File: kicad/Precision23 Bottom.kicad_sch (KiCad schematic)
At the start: 13 parts, among them J396 STANDOFF, J397 STANDOFF, J398 STANDOFF, J399 STANDOFF, J507 Conn_01x06, J895 USB A Male to Blank, U801 Arduino Nano 33 IoT, U802 TXS0108EPW

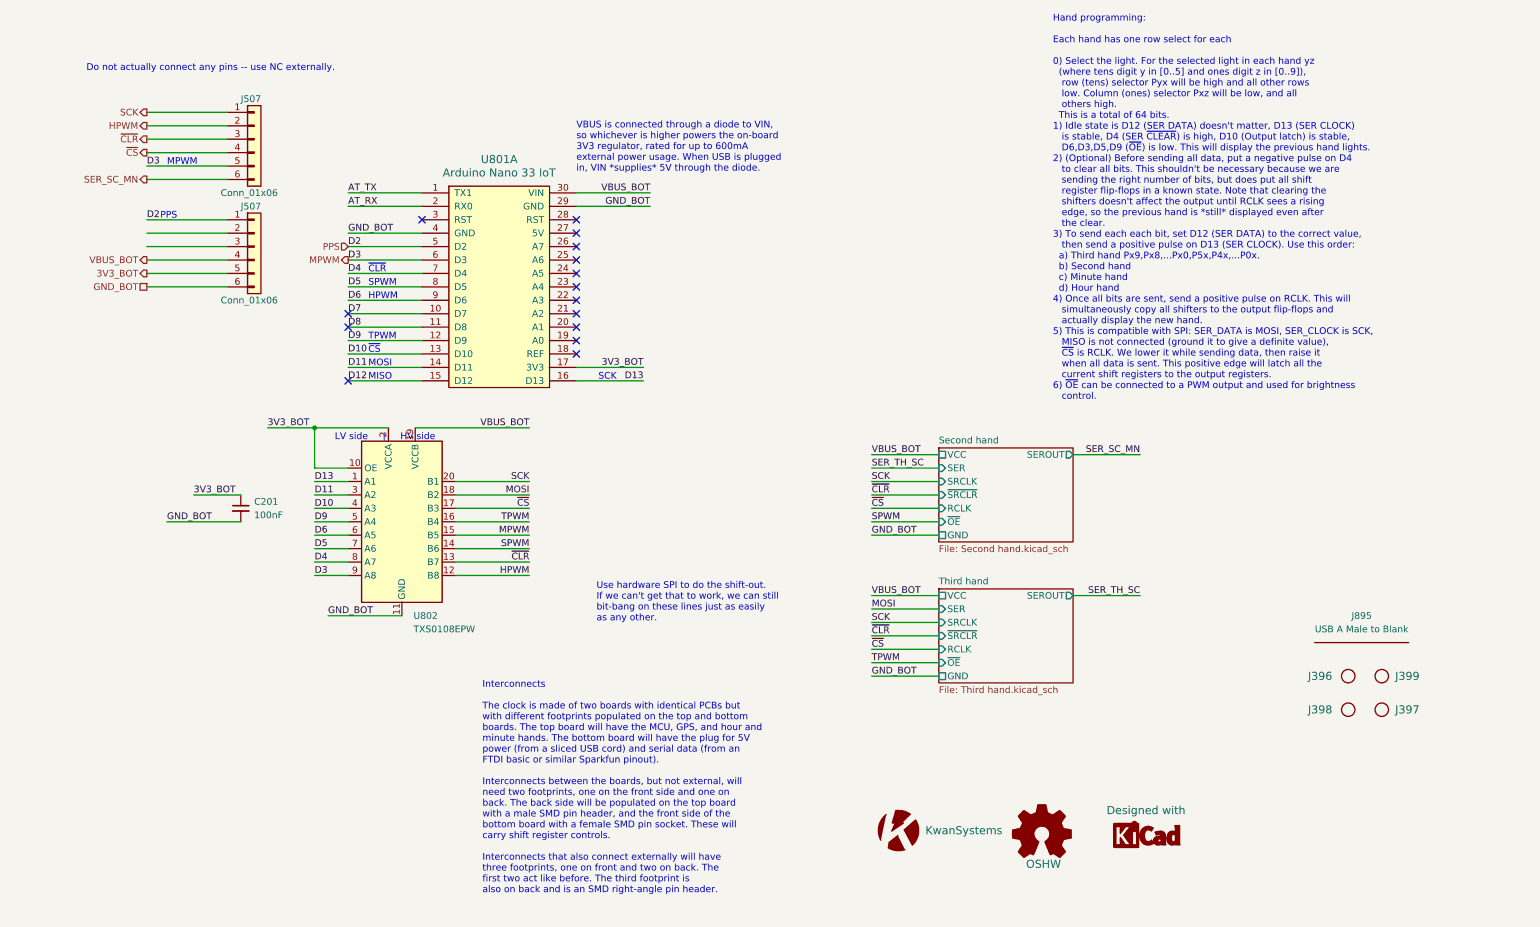
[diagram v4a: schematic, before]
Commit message: Continue wiring MOSFET switches
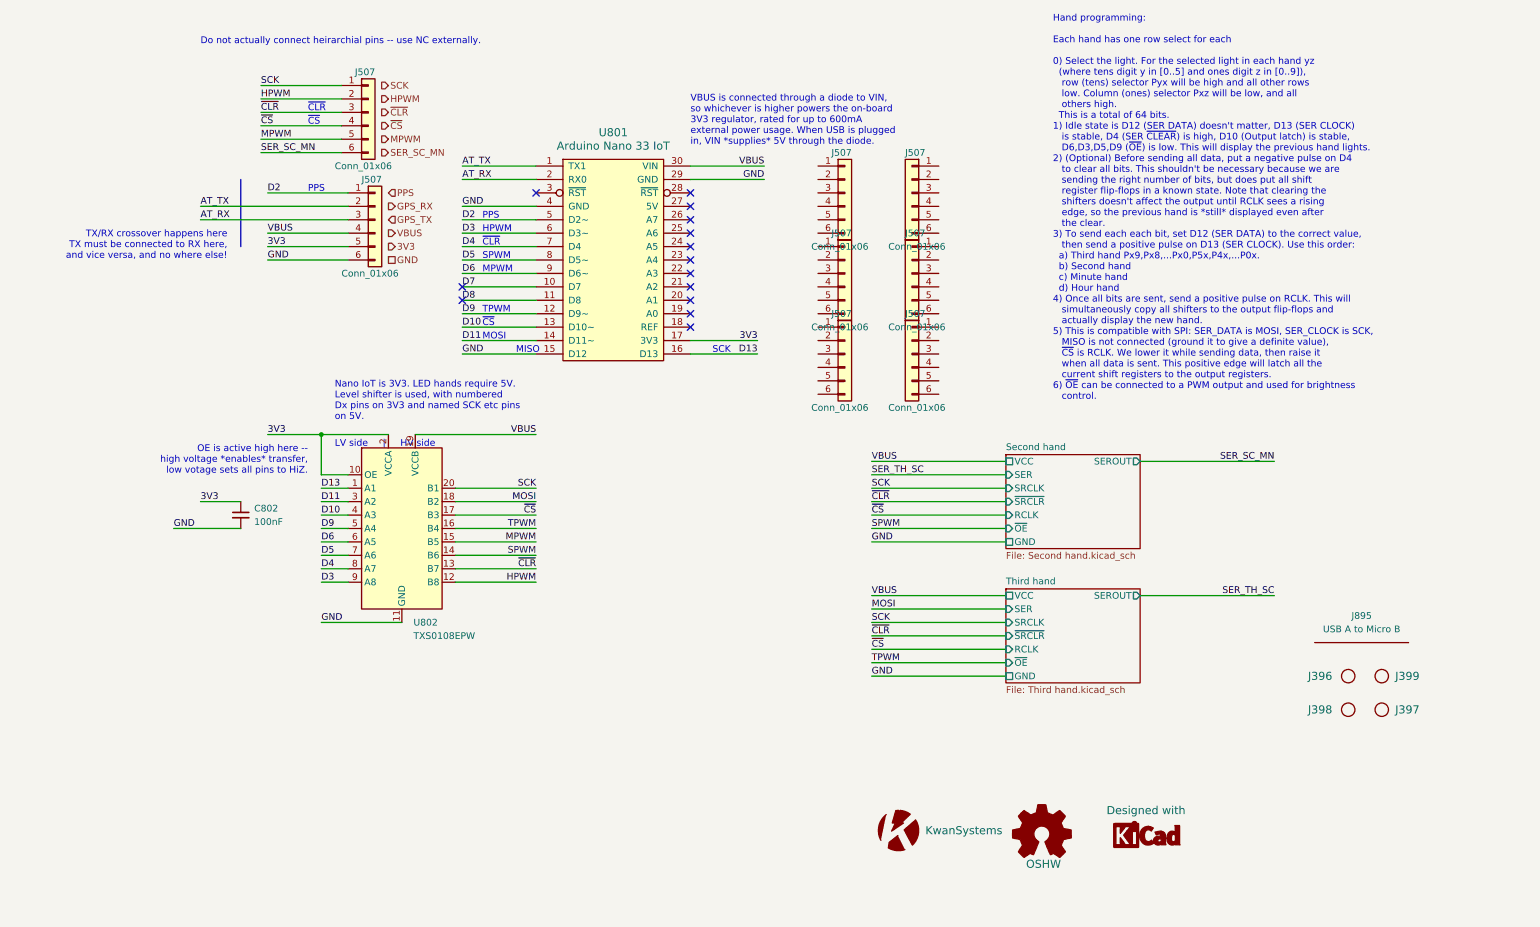
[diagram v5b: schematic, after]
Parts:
- added J507 (x6): Conn_01x06, Connector_PinSocket_2.54mm:PinSocket_1x06_P2.54mm_Vertical_SMD_Pin1Left, symbol Connector_Generic:Conn_01x06
- J895: value USB A Male to Blank -> USB A to Micro B; now left out of the parts list
- U801: footprint KwanSystems:NanoCastellated -> KwanSystems:NanoSMTSocket; Digikey (none) -> 1050-ABX00032-ND; Part Number (none) -> ABX00032; Purpose (none) -> Controller
- U802: Digikey (none) -> 296-23011-1-ND; Part Number (none) -> TXS0108EPWR; Purpose (none) -> Level Shifter
- renumbered C201 to C802
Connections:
- net GND_BOT is gone; now on net GND: C802.2, J507.6 (Pin_6), U801.29 (GND), U801.4 (GND), U802.11 (GND)
- net AT_RX: now also J507.3 (Pin_3)
- net AT_TX: now also J507.2 (Pin_2)
- net MPWM: no longer U801.6 (D3), U802.9 (A8)
- net PPS: no longer J507.1 (Pin_1), U801.5 (D2)
- net 3V3_BOT renamed 3V3
- net D12 renamed GND
- net VBUS_BOT renamed VBUS
- new net D2: J507.1 (Pin_1), U801.5 (D2~)
- new net D3: U801.6 (D3~), U802.9 (A8)
- no-connect marks 15 -> 14
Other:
- note added: "Do not actually connect heirarchial pins -- use NC externally."
- note added: "Nano IoT is 3V3. LED hands require 5V. Level shifter is used, with numbered Dx pins on 3V3 and named SCK etc pins on 5V."
- note added: "OE is active high here -- high voltage *enables* transfer, low votage sets all pins to HiZ."
- note added: "TX/RX crossover happens here TX must be connected to RX here, and vice versa, and no where else!"
- note removed: "Do not actually connect any pins -- use NC externally."
- note removed: "Interconnects The clock is made of two boards with identical PCBs but with different footprints populated on the top and bottom boards. The top board will have the MCU, GPS, and hour and minute hands. The bottom board will have the plug for 5V power (from a sliced USB cord) and serial data (from an FTDI basic or similar Sparkfun pinout). Interconnects between the boards, but not external, will ne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"
- note removed: "Use hardware SPI to do the shift-out. If we can't get that to work, we can still bit-bang on these lines just as easily as any other."
- moved on the sheet: C802, J507, U802

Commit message: Matrix8x8 stuff
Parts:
- added J507 (x2): Conn_01x06, Connector_PinSocket_2.54mm:PinSocket_1x06_P2.54mm_Vertical_SMD_Pin1Left, symbol Connector_Generic:Conn_01x06
- added J810: SolderJumper_3, Jumper:SolderJumper-3_P1.3mm_Open_RoundedPad1.0x1.5mm, symbol Jumper:SolderJumper_3_Open
- added J811: SolderJumper_2, Jumper:SolderJumper-2_P1.3mm_Open_RoundedPad1.0x1.5mm, symbol Jumper:SolderJumper_2_Open
- added U501: SAM-M10Q, RF_GPS:ublox_SAM-M8Q, symbol RF_GPS:SAM-M8Q
- C802: Digikey 445-5613-1-ND -> 445-5666-1-ND; Part Number CGA2B1X7R1C104K050BC -> CGA3E2X7R1H104K080AA
- G102: footprint KwanSystems:StKwansSoldermask -> KwanSystems:PrecisionKwan
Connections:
- net 3V3: now also J507.5 (Pin_5), U501.17 (VCC), U501.2 (VCC_IO), U501.3 (V_BCKP)
- net AT_RX: now also J507.2 (Pin_2), J507.2 (Pin_2), U501.13 (TXD); no longer J507.3 (Pin_3)
- net AT_TX: now also J507.1 (Pin_1), J507.1 (Pin_1), U501.14 (RXD); no longer J507.2 (Pin_2)
- net D10: now also U802.7 (A6); no longer U802.4 (A3)
- net D11: now also U802.8 (A7); no longer U802.3 (A2)
- net D13: now also U802.9 (A8); no longer U802.1 (A1)
- net D2: now also J507.3 (Pin_3), J507.3 (Pin_3), U501.7 (TIMEPULSE); no longer J507.1 (Pin_1)
- net D3: now also U802.1 (A1); no longer U802.9 (A8)
- net D4: no longer U802.8 (A7)
- net D5: now also U802.4 (A3); no longer U802.7 (A6)
- net D6: now also U802.5 (A4); no longer U802.6 (A5)
- net D9: now also U802.6 (A5); no longer U802.5 (A4)
- net GND: now also J507.6 (Pin_6), U501.1 (GND), U501.10 (GND), U501.11 (GND), U501.15 (GND), U501.16 (GND), U501.20 (GND), U501.4 (GND), U501.5 (GND), U501.6 (GND)
- net HPWM: now also U802.17 (B3), J507.2 (Pin_2); no longer U802.12 (B8)
- net MOSI: now also U802.13 (B7), J810.3 (B); no longer U802.18 (B2)
- net MPWM: now also J507.3 (Pin_3), U802.16 (B4), J507.3 (Pin_3); no longer J507.5 (Pin_5), U802.15 (B5)
- net SCK: now also J507.5 (Pin_5), U802.12 (B8), J507.5 (Pin_5); no longer J507.1 (Pin_1), U802.20 (B1)
- net SER_SC_MN: now also J811.1 (A); no longer J507.6 (Pin_6)
- net SPWM: now also U802.20 (B1); no longer U802.14 (B6)
- net TPWM: now also U802.15 (B5); no longer U802.16 (B4)
- net VBUS: now also J507.1 (Pin_1), J507.1 (Pin_1); no longer J507.4 (Pin_4)
- net ~{CS}: now also U802.14 (B6), J507.4 (Pin_4); no longer U802.17 (B3)
- removed net ~{CLR}: J507.3 (Pin_3), U802.13 (B7)
- new net CASCADE: J507.6 (Pin_6), J507.6 (Pin_6), J810.1 (A), J811.2 (B)
- new net Third hand/SER: J810.2 (C)
- no-connect marks 14 -> 60
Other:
- sheet Second hand ports: added none; removed ~{SRCLR}
- sheet Third hand ports: added none; removed ~{SRCLR}
- note added: "Bridge for back"
- note added: "Bridge for back board"
- note added: "Bridge for front"
- note added: "~{SAFEBOOT}, ~{RESET}, SDA, SCL, EXTINT all have internal pullups"
- note removed: "~{CLR}"
- moved on the sheet: J507
